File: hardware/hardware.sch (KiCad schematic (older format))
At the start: 22 parts, among them J1 Conn_01x05_Male, J2 DIN-5_180degree, SW1 SW_Push, SW2 SW_Push, U1 Teensy3.2, U2 TeensyAudioShield3.2, U3 6N138

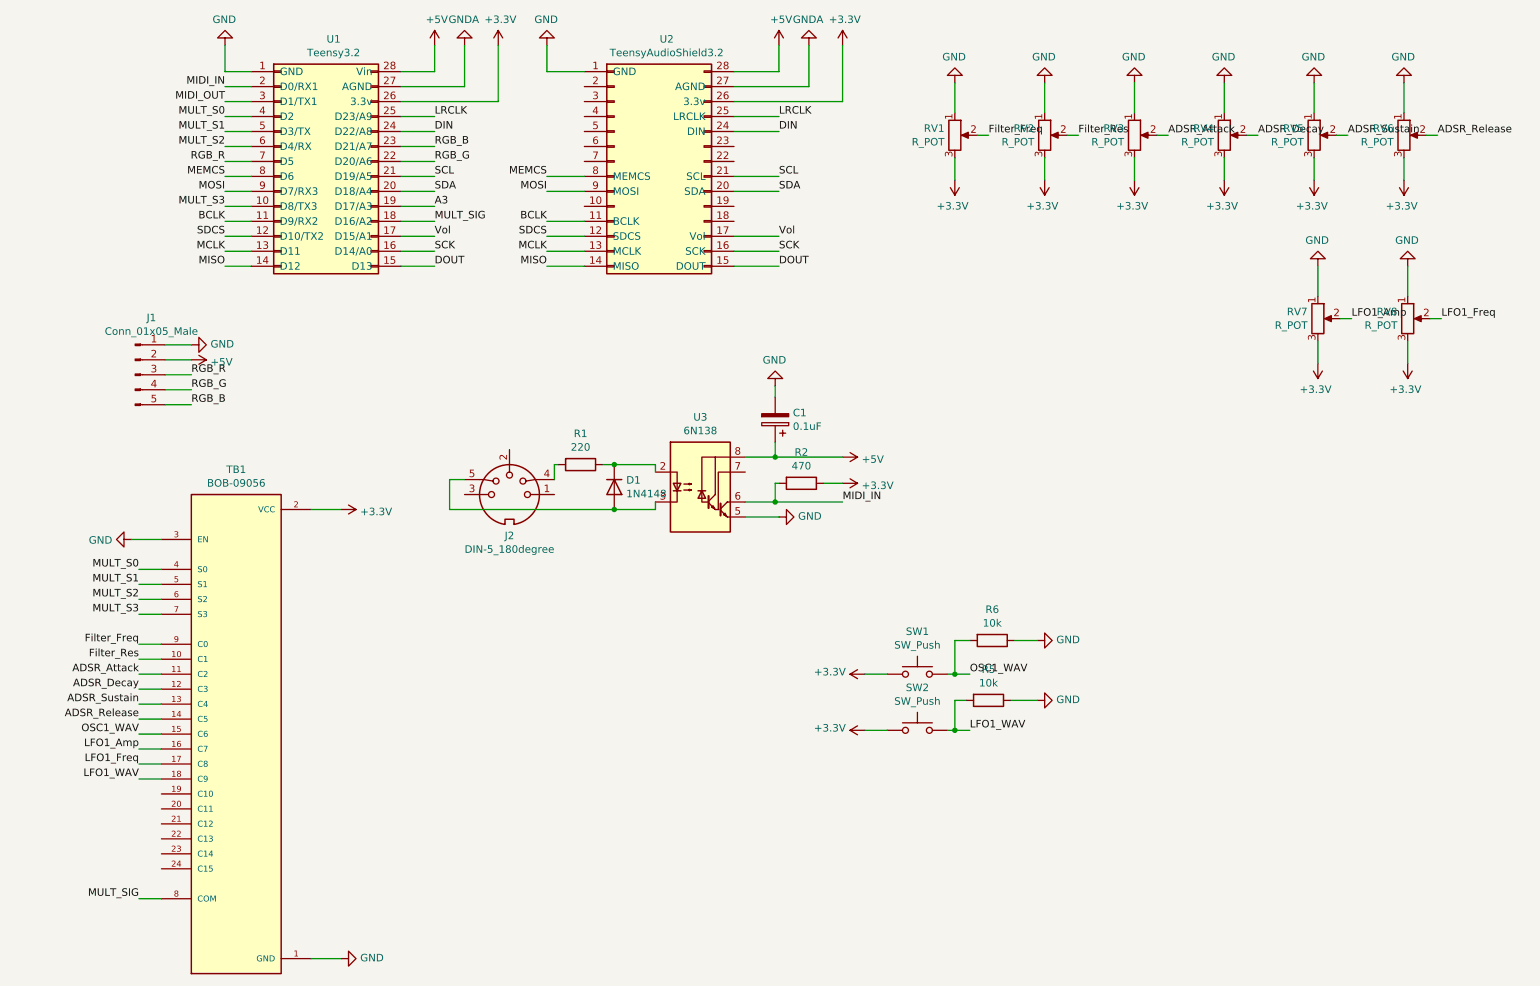
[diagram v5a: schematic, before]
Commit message: V0.5 PCB for Hammond case with pcb mount pots
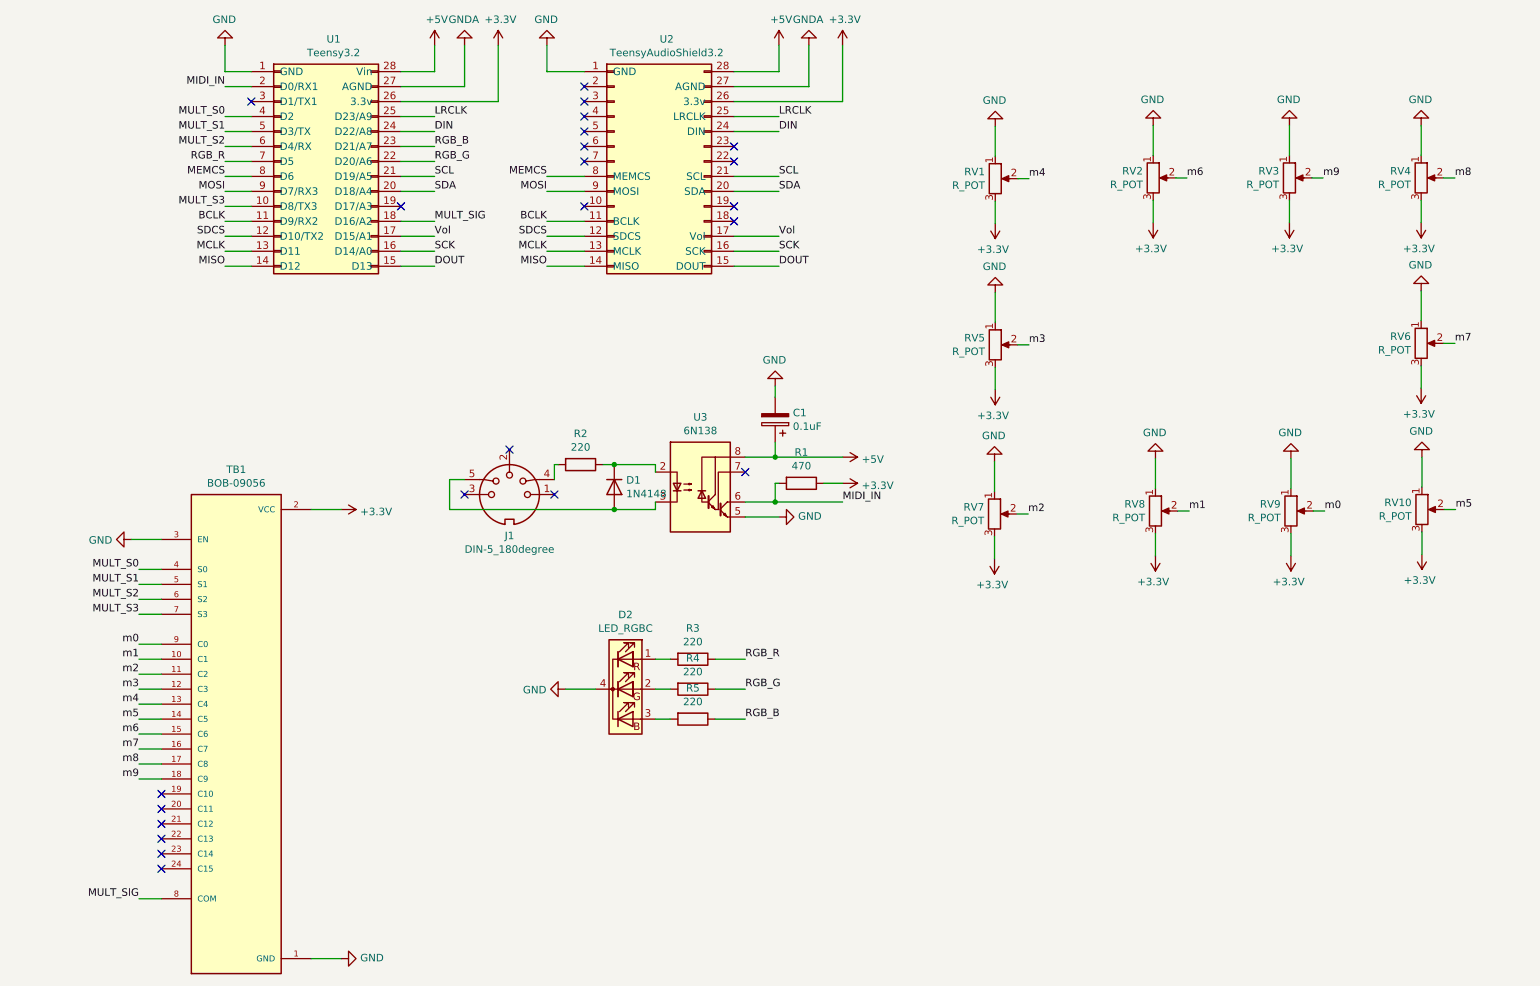
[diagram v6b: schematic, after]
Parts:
- removed J1: Conn_01x05_Male, Connector_PinHeader_2.54mm:PinHeader_1x05_P2.54mm_Vertical, symbol Connector:Conn_01x05_Male
- removed R6: 10k, Resistor_THT:R_Axial_DIN0207_L6.3mm_D2.5mm_P10.16mm_Horizontal, symbol Device:R
- removed SW1, SW2: SW_Push, Connector_PinHeader_2.54mm:PinHeader_1x02_P2.54mm_Vertical, symbol Switch:SW_Push
- added D2: LED_RGBC, LED_THT:LED_D5.0mm-4_RGB, symbol Device:LED_RGBC
- added R3, R4: 220, Resistor_THT:R_Axial_DIN0207_L6.3mm_D2.5mm_P10.16mm_Horizontal, symbol Device:R
- added RV2, RV3: R_POT, Potentiometer_THT:Potentiometer_Alpha_RD901F-40-00D_Single_Vertical_CircularHoles, symbol Device:R_POT
- R5: value 10k -> 220
- RV1: renamed from RV5; footprint Connector_PinHeader_2.54mm:PinHeader_1x03_P2.54mm_Vertical -> Potentiometer_THT:Potentiometer_Alpha_RD901F-40-00D_Single_Vertical_CircularHoles; Name (none) -> ADSR_A
- RV10: renamed from RV6; footprint Connector_PinHeader_2.54mm:PinHeader_1x03_P2.54mm_Vertical -> Potentiometer_THT:Potentiometer_Alpha_RD901F-40-00D_Single_Vertical_CircularHoles; Name (none) -> LFO1_Amp
- RV4: renamed from RV8; footprint Connector_PinHeader_2.54mm:PinHeader_1x03_P2.54mm_Vertical -> Potentiometer_THT:Potentiometer_Alpha_RD901F-40-00D_Single_Vertical_CircularHoles; Name (none) -> ADSR_R
- RV5: renamed from RV4; footprint Connector_PinHeader_2.54mm:PinHeader_1x03_P2.54mm_Vertical -> Potentiometer_THT:Potentiometer_Alpha_RD901F-40-00D_Single_Vertical_CircularHoles; Name (none) -> Filter_Freq
- RV6: renamed from RV7; footprint Connector_PinHeader_2.54mm:PinHeader_1x03_P2.54mm_Vertical -> Potentiometer_THT:Potentiometer_Alpha_RD901F-40-00D_Single_Vertical_CircularHoles; LFO (none) -> LFO1_Freq
- RV7: renamed from RV3; footprint Connector_PinHeader_2.54mm:PinHeader_1x03_P2.54mm_Vertical -> Potentiometer_THT:Potentiometer_Alpha_RD901F-40-00D_Single_Vertical_CircularHoles; Name (none) -> Filter_Res
- RV8: renamed from RV2; footprint Connector_PinHeader_2.54mm:PinHeader_1x03_P2.54mm_Vertical -> Potentiometer_THT:Potentiometer_Alpha_RD901F-40-00D_Single_Vertical_CircularHoles; Name (none) -> OSC1_WAVE
- RV9: renamed from RV1; footprint Connector_PinHeader_2.54mm:PinHeader_1x03_P2.54mm_Vertical -> Potentiometer_THT:Potentiometer_Alpha_RD901F-40-00D_Single_Vertical_CircularHoles; Name (none) -> LFO1_WAVE
- renumbered J2 to J1, R2 to R1, R1 to R2
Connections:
- net +3V3: now also RV2.3, RV3.3
- net GND: now also D2.4 (K), RV2.1, RV3.1; no longer R5.1
- net RGB_B: now also R5.1
- net RGB_G: now also R4.1
- net RGB_R: now also R3.1
- net A3: no longer names the net of U1.19 (D17/A3)
- net ADSR_Attack renamed m2
- net ADSR_Decay renamed m3
- net ADSR_Release renamed m5
- net ADSR_Sustain renamed m4
- net Filter_Freq renamed m0
- net Filter_Res renamed m1
- net LFO1_Amp renamed m7
- net LFO1_Freq renamed m8
- net LFO1_WAV: no longer names the net of R5.2
- net LFO1_WAV: now also D2.3 (BA); no longer TB1.18 (C9)
- net MIDI_OUT: no longer names the net of U1.3 (D1/TX1)
- net OSC1_WAV renamed m6
- net m6: now also RV2.2
- new net: D2.1 (RA), R3.2
- new net: D2.2 (GA), R4.2
- new net m9: RV3.2, TB1.18 (C9)
- no-connect marks 0 -> 23
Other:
- moved on the sheet: RV1, RV10, RV4, RV5, RV6, RV7, RV8, RV9

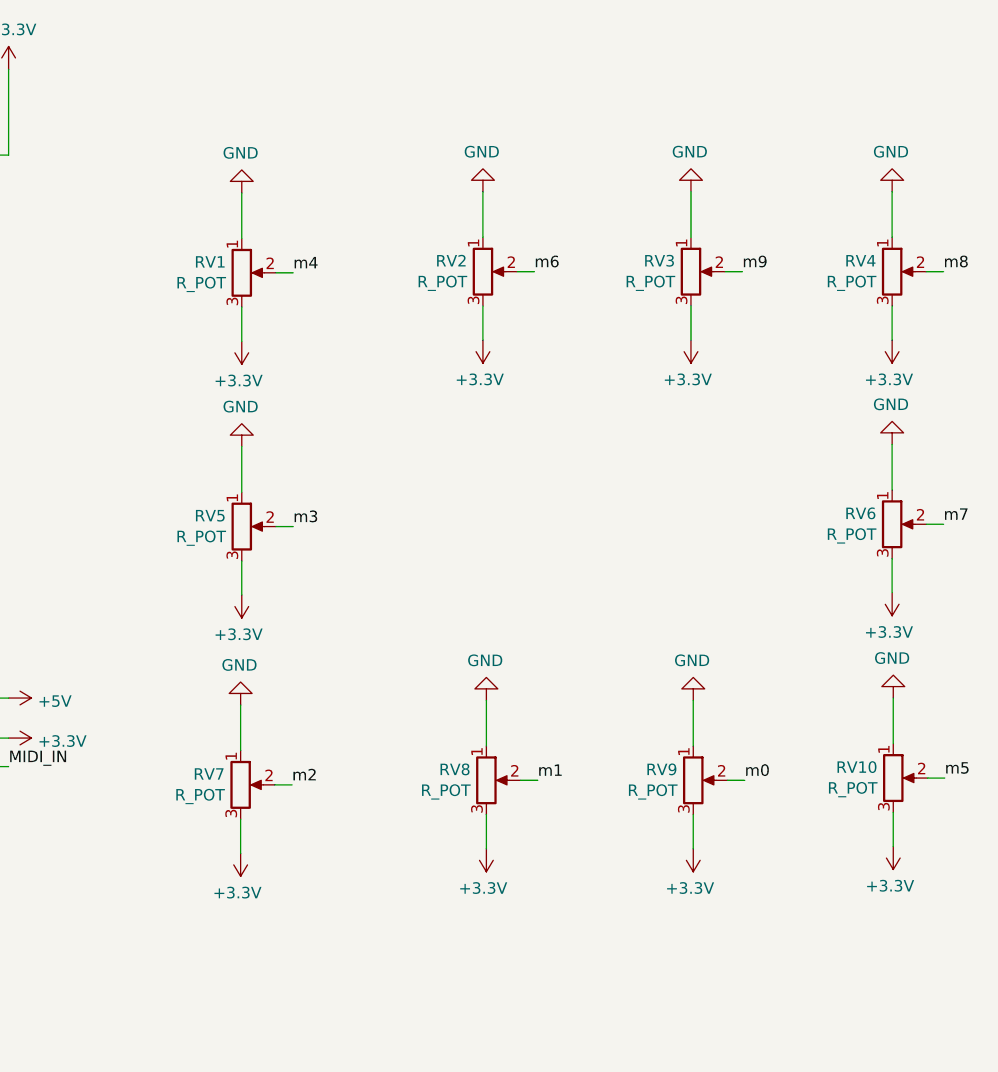
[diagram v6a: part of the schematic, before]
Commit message: Redesign board to allow space for connectors
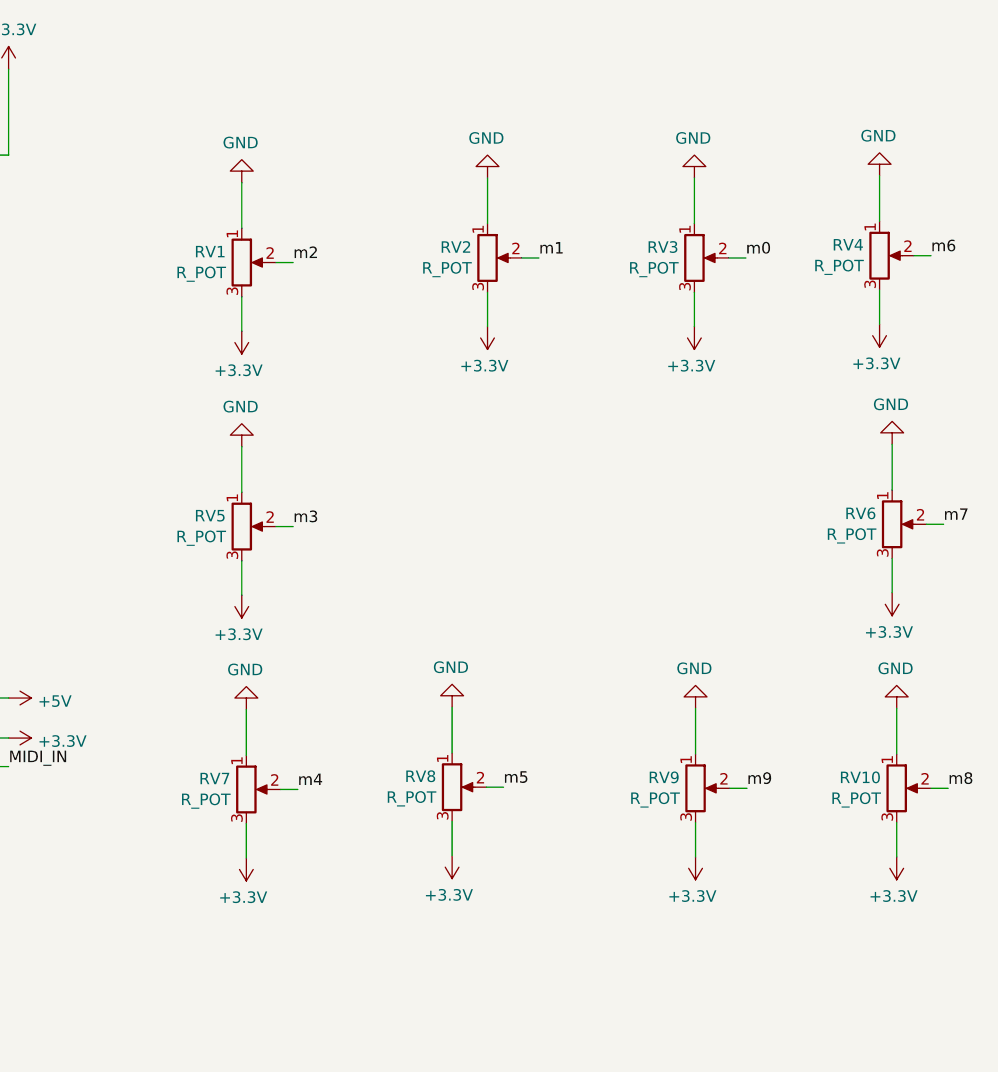
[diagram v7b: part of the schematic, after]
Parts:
- RV1: renamed from RV7; Name Filter_Res -> ADSR_A
- RV10: renamed from RV4; Name ADSR_R -> LFO1_Amp
- RV2: renamed from RV8; Name OSC1_WAVE -> ADSR_D
- RV3: renamed from RV9; Name LFO1_WAVE -> ADSR_S
- RV4: renamed from RV2; Name ADSR_D -> ADSR_R
- RV7: renamed from RV1; Name ADSR_A -> Filter_Res
- RV8: renamed from RV10; Name LFO1_Amp -> OSC1_WAVE
- RV9: renamed from RV3; Name ADSR_S -> LFO1_WAVE
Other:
- moved on the sheet: RV1, RV10, RV2, RV3, RV4, RV7, RV8, RV9

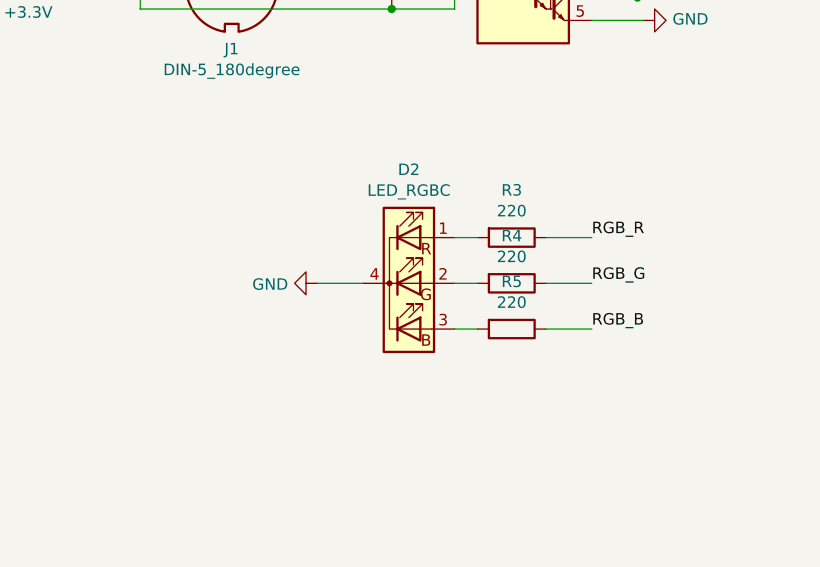
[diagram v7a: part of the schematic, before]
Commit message: Make footprint match LED pinout even if schematic looks wrong
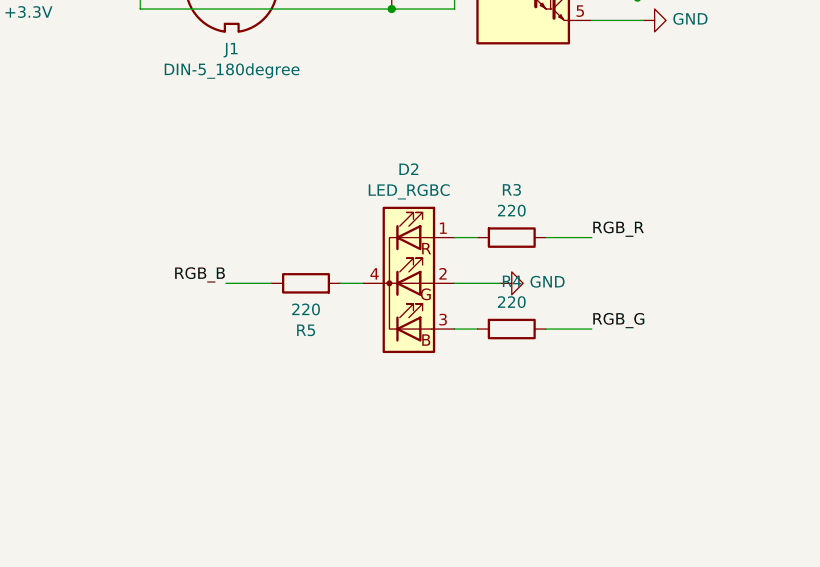
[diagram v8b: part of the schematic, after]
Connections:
- net GND: now also D2.2 (GA); no longer D2.4 (K)
- net at R4.2: now also D2.3 (BA); no longer D2.2 (GA)
- net at R5.2: now also D2.4 (K); no longer D2.3 (BA)
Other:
- moved on the sheet: R4, R5
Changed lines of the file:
@@
-	0    1    1    0
-$EndComp
-$Comp
-L Device:R R4
-U 1 1 5FCD0BCE
-P 5250 5550
-F 0 "R4" V 5043 5550 50  0000 C CNN
-F 1 "220" V 5134 5550 50  0000 C CNN
-F 2 "Resistor_THT:R_Axial_DIN0207_L6.3mm_D2.5mm_P10.16mm_Horizontal" V 5180 5550 50  0001 C CNN
-F 3 "~" H 5250 5550 50  0001 C CNN
-	1    5250 5550
-	0    1    1    0
-$EndComp
-$Comp
-L Device:R R5
-U 1 1 5FCD61B6
-P 5250 5750
-F 0 "R5" V 5043 5750 50  0000 C CNN
-F 1 "220" V 5134 5750 50  0000 C CNN
-F 2 "Resistor_THT:R_Axial_DIN0207_L6.3mm_D2.5mm_P10.16mm_Horizontal" V 5180 5750 50  0001 C CNN
-F 3 "~" H 5250 5750 50  0001 C CNN
-	1    5250 5750
-	0    1    1    0
-$EndComp
-$Comp
-L power:GND #PWR0131
-U 1 1 5FCDFF2C
-P 4400 5550
-F 0 "#PWR0131" H 4400 5300 50  0001 C CNN
-F 1 "GND" V 4405 5422 50  0000 R CNN
-F 2 "" H 4400 5550 50  0001 C CNN
-F 3 "" H 4400 5550 50  0001 C CNN
-	1    4400 5550
 	0    1    1    0
 $EndComp
 Text Label 5600 5350 0    50   ~ 0
 RGB_R
-Text Label 5600 5550 0    50   ~ 0
-RGB_G
-Text Label 5600 5750 0    50   ~ 0
-RGB_B
-Wire Wire Line
-	4400 5550 4600 5550
 Wire Wire Line
 	5000 5350 5100 5350
 Wire Wire Line
-	5000 5550 5100 5550
-Wire Wire Line
-	5100 5750 5000 5750
-Wire Wire Line
-	5400 5750 5600 5750
-Wire Wire Line
-	5600 5550 5400 5550
+	4500 5550 4600 5550
 Wire Wire Line
 	5600 5350 5400 5350
@@
 NoConn ~ 3300 2325
 NoConn ~ 2300 1625
+Wire Wire Line
+	5000 5750 5100 5750
+Wire Wire Line
+	5600 5750 5400 5750
+Text Label 5600 5750 0    50   ~ 0
+RGB_G
+$Comp
+L Device:R R4
+U 1 1 5FCD0BCE
+P 5250 5750
+F 0 "R4" V 5043 5750 50  0000 C CNN
+F 1 "220" V 5134 5750 50  0000 C CNN
+F 2 "Resistor_THT:R_Axial_DIN0207_L6.3mm_D2.5mm_P10.16mm_Horizontal" V 5180 5750 50  0001 C CNN
+F 3 "~" H 5250 5750 50  0001 C CNN
+	1    5250 5750
+	0    1    1    0
+$EndComp
+Wire Wire Line
+	5200 5550 5000 5550
+$Comp
+L power:GND #PWR0131
+U 1 1 5FCDFF2C
+P 5200 5550
+F 0 "#PWR0131" H 5200 5300 50  0001 C CNN
+F 1 "GND" V 5205 5422 50  0000 R CNN
+F 2 "" H 5200 5550 50  0001 C CNN
+F 3 "" H 5200 5550 50  0001 C CNN
+	1    5200 5550
+	0    -1   -1   0
+$EndComp
+Wire Wire Line
+	4200 5550 4000 5550
+Text Label 4000 5550 2    50   ~ 0
+RGB_B
+$Comp
+L Device:R R5
+U 1 1 5FCD61B6
+P 4350 5550
+F 0 "R5" V 4143 5550 50  0000 C CNN
+F 1 "220" V 4234 5550 50  0000 C CNN
+F 2 "Resistor_THT:R_Axial_DIN0207_L6.3mm_D2.5mm_P10.16mm_Horizontal" V 4280 5550 50  0001 C CNN
+F 3 "~" H 4350 5550 50  0001 C CNN
+	1    4350 5550
+	0    -1   -1   0
+$EndComp
 $EndSCHEMATC
